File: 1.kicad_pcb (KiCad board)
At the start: 2 copper layers, 85.1 x 45.7 mm, 50 parts, among them J1 USB_B_Micro, J10 SPI2, J11 Micro_SD_Card, J12 Conn_01x04, J2 Power, J3 SWD, J4 Conn_01x02, J5 ADC, J6 SPI1, J7 UART1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

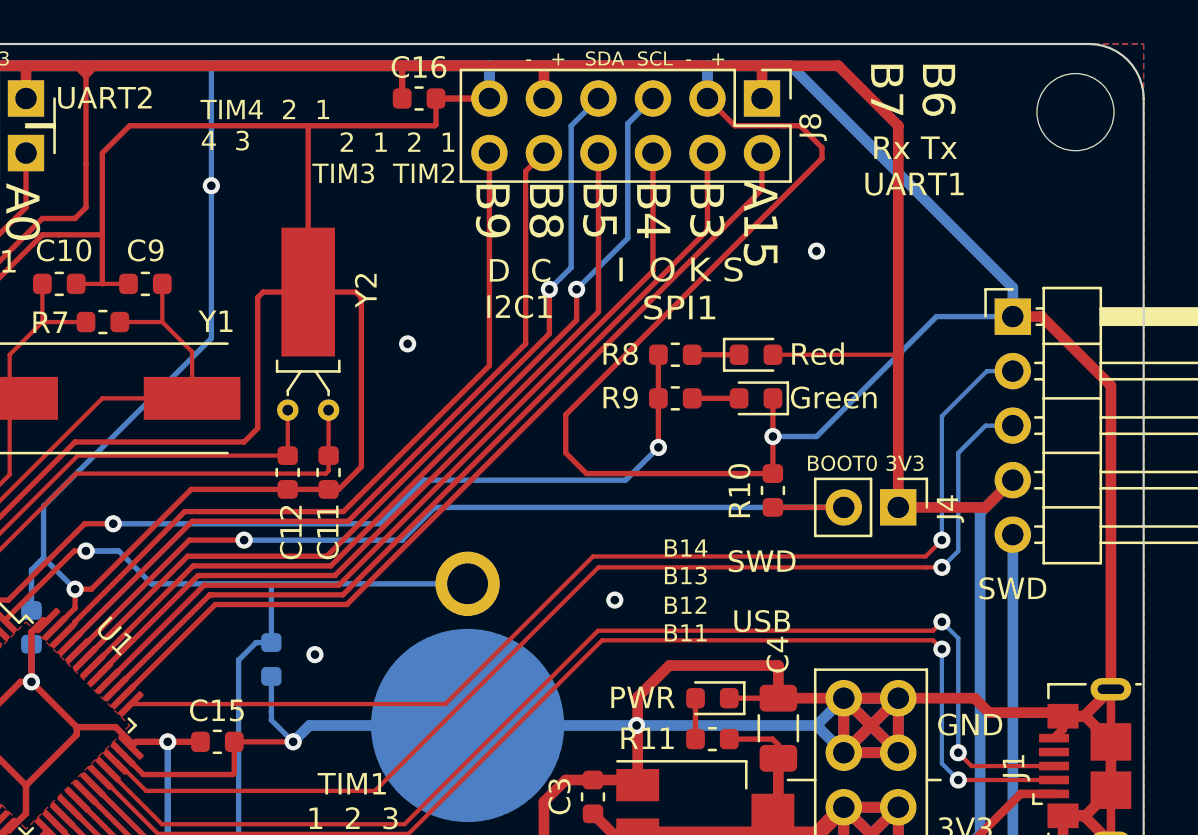
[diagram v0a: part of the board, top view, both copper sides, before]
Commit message: USB D+ 1.5k up res, 104 cap near SWD
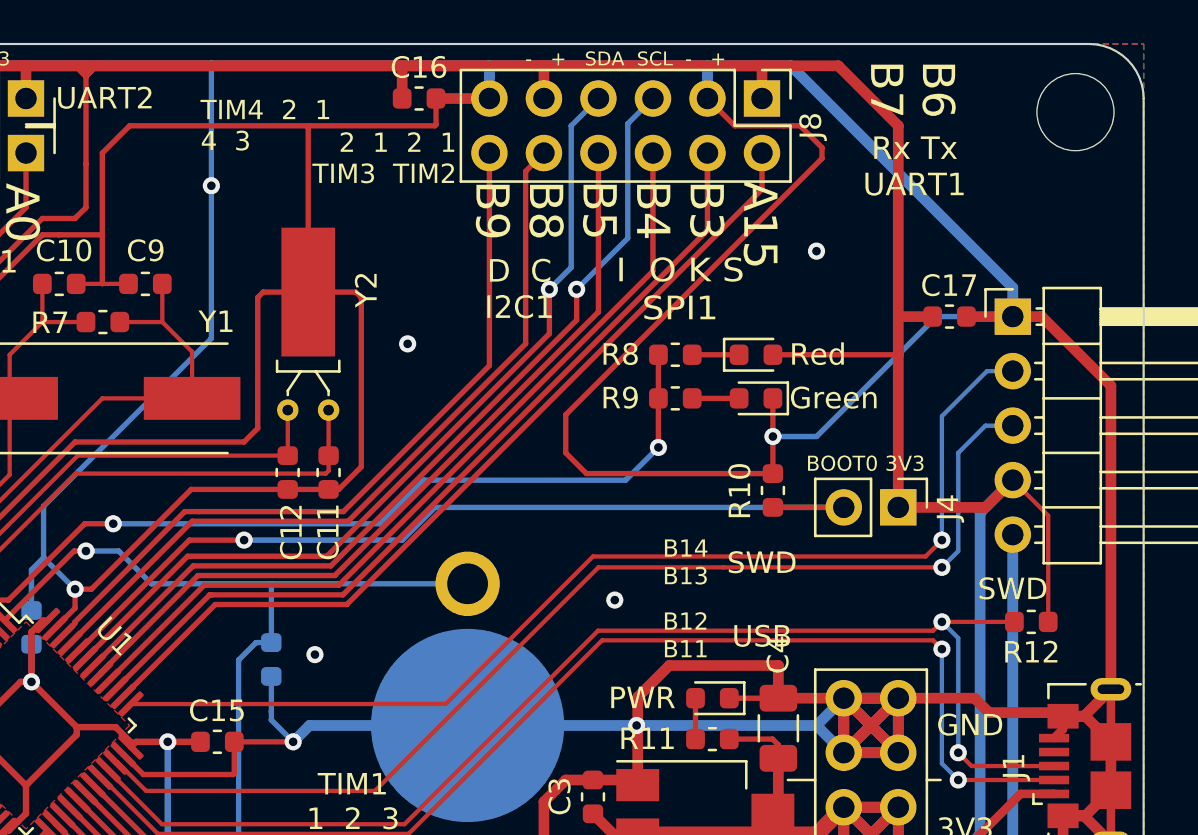
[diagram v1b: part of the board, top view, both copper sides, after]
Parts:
- added C17: 104, Capacitor_SMD:C_0603_1608Metric, F.Cu at (172.6, 99.1)
- added R12: 1.5k, Resistor_SMD:R_0603_1608Metric, F.Cu at (176.4, 113.3)
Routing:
- net +3V3: track 390.1 -> 399.5 mm
- net /USB_D+: track 54.9 -> 58.3 mm
- net GND: track 703.4 -> 705.5 mm

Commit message: op power lines 0.29mm
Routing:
- net +3V3: track 399.5 -> 397.3 mm
- net GND: track 705.5 -> 704.6 mm
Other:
- board text added: "I2C1"

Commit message: relink GND line near 32.768k OSC
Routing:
- net GND: track 704.6 -> 702.8 mm
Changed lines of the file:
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@@
   (segment (start 170.18 116.84) (end 173.736 116.84) (width 0.5) (layer F.Cu) (net 2))
   (segment (start 180.086 116.425) (end 180.086 102.282) (width 0.5) (layer F.Cu) (net 2))
-  (segment (start 134.074322 119.462342) (end 134.074322 119.497682) (width 0.25) (layer F.Cu) (net 2))
   (segment (start 178.891 122.32) (end 180.086 121.125) (width 0.5) (layer F.Cu) (net 2))
   (segment (start 177.856 122.32) (end 178.891 122.32) (width 0.5) (layer F.Cu) (net 2))
@@
   (segment (start 171.166002 131.064) (end 174.132008 128.097994) (width 0.5) (layer F.Cu) (net 2))
   (segment (start 164.592 131.064) (end 171.166002 131.064) (width 0.5) (layer F.Cu) (net 2))
-  (segment (start 134.074322 119.462342) (end 134.109664 119.462342) (width 0.25) (layer F.Cu) (net 2))
   (segment (start 129.794 110.85937) (end 130.359685 110.293685) (width 0.25) (layer B.Cu) (net 2))
   (segment (start 129.794 112.7505) (end 129.794 110.85937) (width 0.25) (layer B.Cu) (net 2))
   (segment (start 148.641 88.9) (end 151.13 88.9) (width 0.5) (layer F.Cu) (net 2))
-  (segment (start 133.096 95.25) (end 133.096 91.44) (width 0.29) (layer F.Cu) (net 2))
-  (segment (start 133.096 91.44) (end 134.366 90.17) (width 0.29) (layer F.Cu) (net 2))
-  (segment (start 148.641 90.119) (end 148.641 88.9) (width 0.29) (layer F.Cu) (net 2))
-  (segment (start 148.59 90.17) (end 148.641 90.119) (width 0.25) (layer F.Cu) (net 2))
-  (segment (start 142.687 90.231) (end 142.748 90.17) (width 0.25) (layer F.Cu) (net 2))
-  (segment (start 142.687 97.917) (end 142.687 90.231) (width 0.25) (layer F.Cu) (net 2))
-  (segment (start 142.748 90.17) (end 148.59 90.17) (width 0.29) (layer F.Cu) (net 2))
-  (segment (start 134.366 90.17) (end 142.748 90.17) (width 0.29) (layer F.Cu) (net 2))
+  (segment (start 148.641 90.119) (end 148.641 88.9) (width 0.25) (layer F.Cu) (net 2))
   (via (at 143.002 114.808) (size 0.8) (drill 0.4) (layers F.Cu B.Cu) (net 2))
   (via (at 166.37 96.012) (size 0.8) (drill 0.4) (layers F.Cu B.Cu) (net 2))
@@
   (segment (start 125.10198 125.73) (end 122.555 125.73) (width 0.29) (layer F.Cu) (net 2))
   (segment (start 128.187658 122.644322) (end 125.10198 125.73) (width 0.29) (layer F.Cu) (net 2))
-  (segment (start 134.081378 119.462342) (end 135.269036 120.65) (width 0.29) (layer F.Cu) (net 2))
-  (segment (start 134.074322 119.462342) (end 134.081378 119.462342) (width 0.29) (layer F.Cu) (net 2))
-  (segment (start 139.243 118.872) (end 139.243 119.837) (width 0.29) (layer F.Cu) (net 2))
-  (segment (start 138.43 120.65) (end 135.269036 120.65) (width 0.29) (layer F.Cu) (net 2))
-  (segment (start 139.243 119.837) (end 138.43 120.65) (width 0.29) (layer F.Cu) (net 2))
   (segment (start 130.683 95.25) (end 133.096 95.25) (width 0.29) (layer F.Cu) (net 2))
   (segment (start 124.77699 101.15601) (end 130.683 95.25) (width 0.29) (layer F.Cu) (net 2))
@@
   (segment (start 126.059284 115.696998) (end 124.77699 114.414704) (width 0.29) (layer F.Cu) (net 2))
   (segment (start 126.066338 115.696998) (end 126.059284 115.696998) (width 0.29) (layer F.Cu) (net 2))
+  (segment (start 135.001 120.396) (end 138.684 120.396) (width 0.29) (layer F.Cu) (net 2))
+  (segment (start 139.243 119.837) (end 139.243 118.872) (width 0.29) (layer F.Cu) (net 2))
+  (segment (start 138.684 120.396) (end 139.243 119.837) (width 0.29) (layer F.Cu) (net 2))
+  (segment (start 134.074322 119.462342) (end 134.081378 119.462342) (width 0.29) (layer F.Cu) (net 2))
+  (segment (start 134.074322 119.469322) (end 135.001 120.396) (width 0.29) (layer F.Cu) (net 2))
+  (segment (start 134.074322 119.462342) (end 134.074322 119.469322) (width 0.29) (layer F.Cu) (net 2))
+  (segment (start 135.89 95.25) (end 138.176 92.964) (width 0.25) (layer F.Cu) (net 2))
+  (segment (start 133.096 95.25) (end 135.89 95.25) (width 0.25) (layer F.Cu) (net 2))
+  (segment (start 141.021 90.119) (end 138.176 92.964) (width 0.25) (layer F.Cu) (net 2))
+  (segment (start 148.641 90.119) (end 141.021 90.119) (width 0.25) (layer F.Cu) (net 2))
+  (segment (start 138.741685 92.964) (end 138.176 92.964) (width 0.25) (layer F.Cu) (net 2))
+  (segment (start 140.984 92.964) (end 138.741685 92.964) (width 0.25) (layer F.Cu) (net 2))
+  (segment (start 142.687 94.667) (end 140.984 92.964) (width 0.25) (layer F.Cu) (net 2))
+  (segment (start 142.687 97.917) (end 142.687 94.667) (width 0.25) (layer F.Cu) (net 2))
   (segment (start 170.18 100.838) (end 170.18 107.95) (width 0.5) (layer F.Cu) (net 3))
   (segment (start 125.712785 116.060785) (end 125.712785 116.050551) (width 0.25) (layer F.Cu) (net 3))
@@
   (segment (start 172.974 105.41) (end 172.974 109.982) (width 0.2) (layer B.Cu) (net 11))
   (segment (start 134.999884 121.09501) (end 133.720769 119.815895) (width 0.2) (layer F.Cu) (net 11))
-  (segment (start 145.85899 121.09501) (end 134.999884 121.09501) (width 0.2) (layer F.Cu) (net 11))
   (segment (start 156.21 110.744) (end 145.85899 121.09501) (width 0.2) (layer F.Cu) (net 11))
   (segment (start 172.212 110.744) (end 156.21 110.744) (width 0.2) (layer F.Cu) (net 11))
+  (segment (start 145.85899 121.09501) (end 134.999884 121.09501) (width 0.2) (layer F.Cu) (net 11))
   (segment (start 167.6145 107.9755) (end 167.64 107.95) (width 0.25) (layer F.Cu) (net 12))
   (segment (start 131.988342 114.636338) (end 137.15068 109.474) (width 0.25) (layer F.Cu) (net 12))
@@
   (segment (start 133.096 102.87) (end 137.278 102.87) (width 0.2) (layer F.Cu) (net 40))
   (segment (start 126.269681 109.696319) (end 133.096 102.87) (width 0.2) (layer F.Cu) (net 40))
-  (segment (start 137.278 100.702) (end 135.89 99.314) (width 0.2) (layer F.Cu) (net 40))
-  (segment (start 137.278 102.87) (end 137.278 100.702) (width 0.2) (layer F.Cu) (net 40))
   (segment (start 126.269681 113.779021) (end 126.269681 109.696319) (width 0.2) (layer F.Cu) (net 40))
   (segment (start 127.126998 114.636338) (end 126.269681 113.779021) (width 0.2) (layer F.Cu) (net 40))
+  (segment (start 137.278 102.87) (end 137.278 100.702) (width 0.2) (layer F.Cu) (net 40))
+  (segment (start 137.278 100.702) (end 135.89 99.314) (width 0.2) (layer F.Cu) (net 40))
   (segment (start 132.334 99.314) (end 130.302 99.314) (width 0.2) (layer F.Cu) (net 41))
   (segment (start 130.302 97.536) (end 130.302 99.314) (width 0.2) (layer F.Cu) (net 41))
@@
   (segment (start 125.73 109.474) (end 128.778 106.426) (width 0.2) (layer F.Cu) (net 41))
   (segment (start 128.778 100.838) (end 128.778 102.87) (width 0.2) (layer F.Cu) (net 41))
-  (segment (start 130.302 99.314) (end 128.778 100.838) (width 0.2) (layer F.Cu) (net 41))
   (segment (start 125.73 113.946446) (end 126.773445 114.989891) (width 0.2) (layer F.Cu) (net 41))
   (segment (start 125.73 109.474) (end 125.73 113.946446) (width 0.2) (layer F.Cu) (net 41))
+  (segment (start 130.302 99.314) (end 128.778 100.838) (width 0.2) (layer F.Cu) (net 41))
   (segment (start 143.637 103.417) (end 143.637 105.537) (width 0.2) (layer F.Cu) (net 42))
   (segment (start 143.51 106.37449) (end 131.87751 106.37449) (width 0.2) (layer F.Cu) (net 42))

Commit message: 视频中修改
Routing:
- net GND: track 702.8 -> 703.6 mm
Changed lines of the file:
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@@
     (thickness 1.6)
     (drawings 83)
-    (tracks 772)
+    (tracks 775)
     (zones 0)
     (modules 52)
@@
   )
   (setup
-    (last_trace_width 0.25)
+    (last_trace_width 0.29)
     (user_trace_width 0.2)
     (user_trace_width 0.29)
@@
     (tags capacitor)
     (attr smd)
-    (fp_text reference C17 (at 0 -1.43) (layer F.SilkS)
+    (fp_text reference C17 (at 0 1.524) (layer F.SilkS)
       (effects (font (size 1 1) (thickness 0.15)))
     )
@@
     (tags capacitor)
     (attr smd)
-    (fp_text reference C4 (at 3.432 0 90) (layer F.SilkS)
+    (fp_text reference C4 (at 2.924 0.889 90) (layer F.SilkS)
       (effects (font (size 1 1) (thickness 0.15)))
     )
@@
     (effects (font (size 1 1) (thickness 0.15)) (justify left))
   )
-  (gr_text SWD (at 175.514 111.76) (layer F.SilkS)
+  (gr_text SWD (at 175.641 96.52) (layer F.SilkS)
     (effects (font (size 1 1) (thickness 0.2)))
   )
@@
   (segment (start 140.335 98.171) (end 140.335 104.267) (width 0.25) (layer F.Cu) (net 2))
   (segment (start 133.096 95.25) (end 133.096 97.536) (width 0.25) (layer F.Cu) (net 2))
-  (segment (start 131.826 112.64202) (end 130.892342 113.575678) (width 0.25) (layer F.Cu) (net 2))
+  (segment (start 131.826 112.64202) (end 130.892342 113.575678) (width 0.29) (layer F.Cu) (net 2))
   (segment (start 132.588 111.76) (end 131.826 111.76) (width 0.25) (layer F.Cu) (net 2))
   (segment (start 137.236 107.112) (end 132.588 111.76) (width 0.25) (layer F.Cu) (net 2))
   (segment (start 131.826 111.76) (end 131.826 111.76) (width 0.25) (layer F.Cu) (net 2))
   (segment (start 141.732 107.112) (end 137.236 107.112) (width 0.25) (layer F.Cu) (net 2))
-  (segment (start 131.826 111.76) (end 131.826 112.64202) (width 0.25) (layer F.Cu) (net 2))
+  (segment (start 131.826 111.76) (end 131.826 112.64202) (width 0.29) (layer F.Cu) (net 2))
   (via (at 131.826 111.76) (size 0.8) (drill 0.4) (layers F.Cu B.Cu) (net 2))
   (segment (start 130.359685 110.293685) (end 131.826 111.76) (width 0.25) (layer B.Cu) (net 2))
@@
   (segment (start 130.683 95.25) (end 133.096 95.25) (width 0.29) (layer F.Cu) (net 2))
   (segment (start 124.77699 101.15601) (end 130.683 95.25) (width 0.29) (layer F.Cu) (net 2))
-  (segment (start 124.77699 114.414704) (end 124.77699 101.15601) (width 0.29) (layer F.Cu) (net 2))
   (segment (start 126.059284 115.696998) (end 124.77699 114.414704) (width 0.29) (layer F.Cu) (net 2))
   (segment (start 126.066338 115.696998) (end 126.059284 115.696998) (width 0.29) (layer F.Cu) (net 2))
@@
   (segment (start 142.687 94.667) (end 140.984 92.964) (width 0.25) (layer F.Cu) (net 2))
   (segment (start 142.687 97.917) (end 142.687 94.667) (width 0.25) (layer F.Cu) (net 2))
+  (segment (start 124.765 111.455) (end 123.952 111.455) (width 0.29) (layer F.Cu) (net 2))
+  (segment (start 124.77699 111.44301) (end 124.765 111.455) (width 0.29) (layer F.Cu) (net 2))
+  (segment (start 124.77699 114.414704) (end 124.77699 111.44301) (width 0.29) (layer F.Cu) (net 2))
+  (segment (start 124.77699 111.44301) (end 124.77699 101.15601) (width 0.29) (layer F.Cu) (net 2))
   (segment (start 170.18 100.838) (end 170.18 107.95) (width 0.5) (layer F.Cu) (net 3))
   (segment (start 125.712785 116.060785) (end 125.712785 116.050551) (width 0.25) (layer F.Cu) (net 3))
@@
   (segment (start 177.433 121.297) (end 177.436 121.3) (width 0.4) (layer F.Cu) (net 4))
   (segment (start 175.883 121.297) (end 177.433 121.297) (width 0.4) (layer F.Cu) (net 4))
-  (segment (start 170.18 127) (end 175.883 121.297) (width 0.4) (layer F.Cu) (net 4))
+  (segment (start 170.18 127) (end 175.883 121.297) (width 0.5) (layer F.Cu) (net 4))
   (segment (start 159.548 127) (end 158.038 125.49) (width 0.75) (layer F.Cu) (net 4))
   (segment (start 164.592 127) (end 159.548 127) (width 0.75) (layer F.Cu) (net 4))

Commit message: tran 90deg
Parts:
- moved J1 130.7 mm to (48.7, 108.6), turned to 270 degrees
- moved J3 127.2 mm to (52.1, 129.5), turned to 180 degrees
- moved R12 125.2 mm to (51.2, 115.3), turned to 0 degrees
- moved C17 121.4 mm to (55.0, 129.5), turned to 180 degrees
- moved J2 116.8 mm to (57.4, 99.1), turned to 0 degrees
- moved J4 113.5 mm to (57.4, 120.7), turned to 90 degrees
- moved J8 112.2 mm to (63.8, 139.7), turned to 90 degrees
- moved C1 105.4 mm to (63.0, 100.2), turned to 90 degrees
- moved D1 103.1 mm to (64.0, 127.8), turned to 180 degrees
- moved D2 102.1 mm to (64.0, 125.7), turned to 0 degrees
- moved R10 102.1 mm to (63.2, 121.4), turned to 270 degrees
- moved C4 101.9 mm to (63.0, 110.4), turned to 270 degrees
- moved U2 96.4 mm to (66.4, 105.4), turned to 180 degrees
- moved R11 95.9 mm to (66.1, 109.9), turned to 0 degrees
- moved R8 95.9 mm to (67.8, 127.8), turned to 0 degrees
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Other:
- outline, holes or cut-outs redrawn
- board text added: "+ - SCL SDA + -"
- board text added: "+ - SDA SCL + -"
- board text added: "1 2 3 4"
- board text added: "3 2 1 TIM1"
- board text added: "3 4 1 2 TIM4"
- board text added: "3V3 GND Rx Tx NSS GND SCK MISO MOSI 3V3"
- board text added: "3V3 MOSI MISO SCK GND NSS"
- board text added: "5V 3V3 GND"
- board text added: "B11 B12"
- board text added: "B13 B14"
- board text added: "GND Rx Tx MCO"
- board text added: "I2C1 D C"
- board text added: "SPI1 S K O I"
- board text added: "TIM2 TIM3 1 2 1 2"
- board text added: "UART3 Rx Tx TIM2 4 3"
- board text removed: "- + SCL SDA - +"
- board text removed: "- + SDA SCL - +"
- board text removed: "2 1 2 1 TIM3 TIM2"
- board text removed: "3 4 TIM2 Tx Rx UART3"
- board text removed: "3V3 MOSI MISO SCK GND NSS Tx Rx GND 3V3"
- board text removed: "4 3 2 1"
- board text removed: "B12 B11"
- board text removed: "B14 B13"
- board text removed: "BOOT0 3V3"
- board text removed: "D C I2C1"
- board text removed: "I O K S SPI1"
- board text removed: "MCO Tx Rx GND"
- board text removed: "NSS GND SCK MISO MOSI 3V3"
- board text removed: "TIM1 1 2 3"
- board text removed: "TIM4 2 1 4 3"

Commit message: lines near power PinHeader
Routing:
- net +3V3: track 397.3 -> 401.0 mm
